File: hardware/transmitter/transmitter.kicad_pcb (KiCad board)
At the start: 2 copper layers, 85.1 x 53.3 mm, 23 parts, among them J1 Screw_Terminal_01x05, P5 Digital, P6 Analog, U1 uA7805, U2 TMP36, U3 JSN-SR04T-2.0, U4 MAX3232

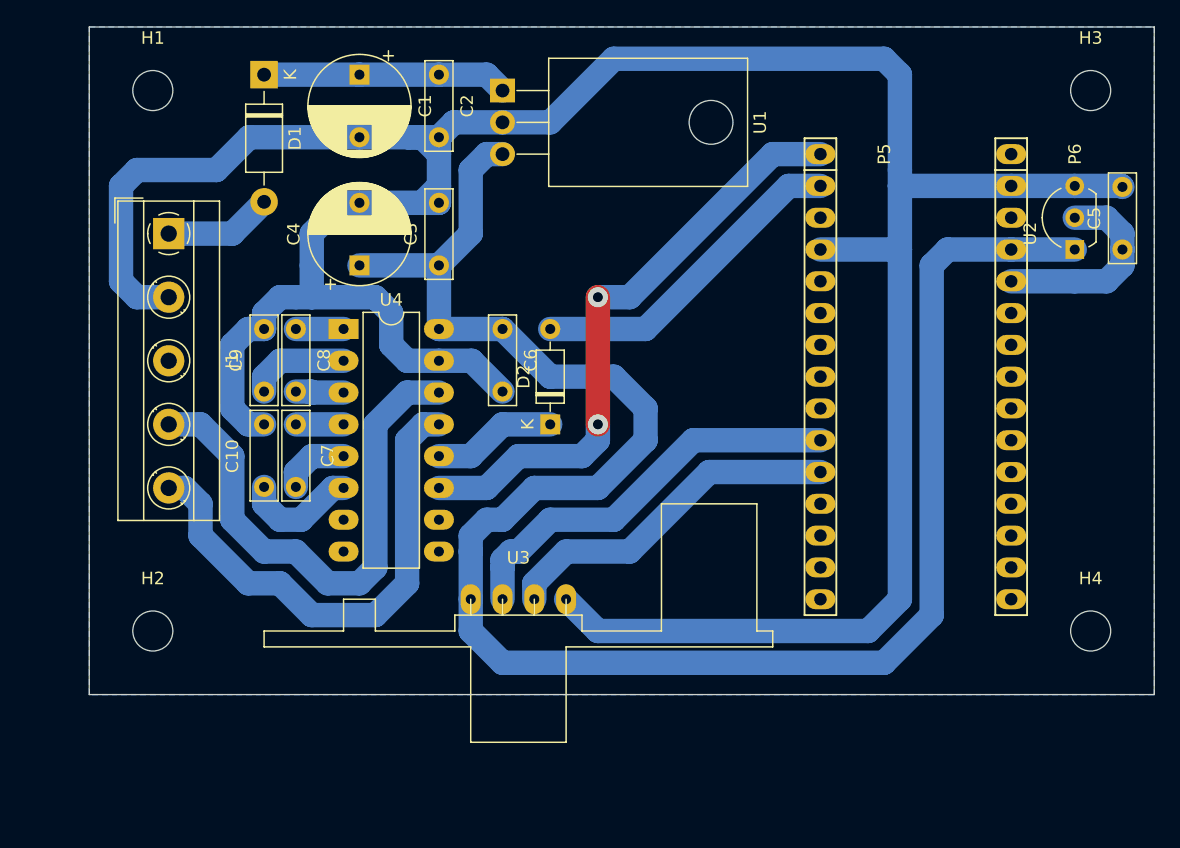
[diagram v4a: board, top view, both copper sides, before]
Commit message: improved silk + additional .pdfs
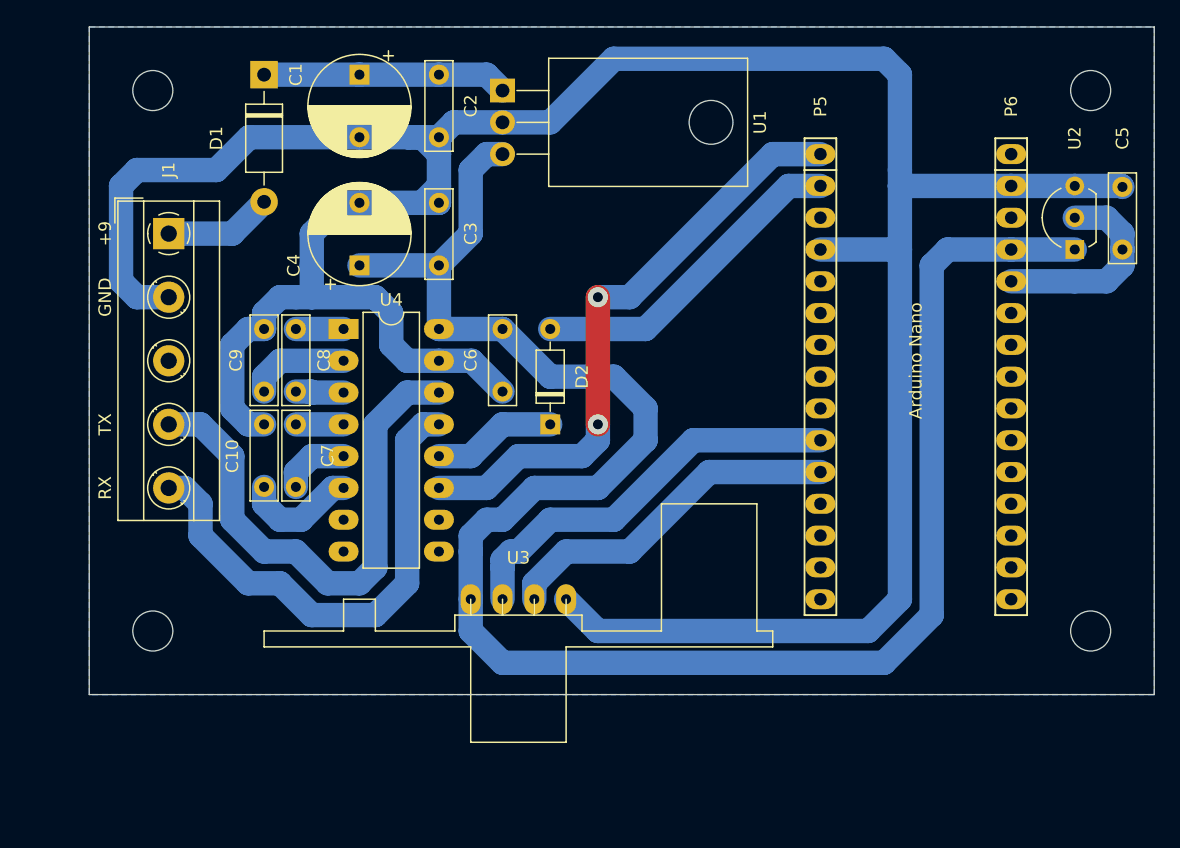
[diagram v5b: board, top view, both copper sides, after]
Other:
- board text added: "+9"
- board text added: "Arduino Nano"
- board text added: "GND"
- board text added: "RX"
- board text added: "TX"
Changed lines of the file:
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@@
   (general
     (thickness 1.6)
-    (drawings 6)
+    (drawings 13)
     (tracks 162)
     (zones 0)
@@
     (44 Edge.Cuts user)
     (45 Margin user)
-    (46 B.CrtYd user)
+    (46 B.CrtYd user hide)
     (47 F.CrtYd user)
-    (48 B.Fab user)
-    (49 F.Fab user)
+    (48 B.Fab user hide)
+    (49 F.Fab user hide)
   )
   (setup
@@
     (descr "TO-92L leads in-line (large body variant of TO-92), also known as TO-226, wide, drill 0.75mm (see https://www.diodes.com/assets/Package-Files/TO92L.pdf and http://www.ti.com/lit/an/snoa059/snoa059.pdf)")
     (tags "TO-92L Inline Wide transistor")
-    (fp_text reference U2 (at 1.27 -3.56 90) (layer F.SilkS)
+    (fp_text reference U2 (at 8.89 0 90) (layer F.SilkS)
       (effects (font (size 1 1) (thickness 0.15)))
     )
@@
     (descr "Through hole socket strip")
     (tags "socket strip")
-    (fp_text reference P6 (at 0 -5.1 90) (layer F.SilkS)
+    (fp_text reference P6 (at -3.81 0 90) (layer F.SilkS)
       (effects (font (size 1 1) (thickness 0.15)))
     )
@@
     (descr "Through hole socket strip")
     (tags "socket strip")
-    (fp_text reference P5 (at 0 -5.1 90) (layer F.SilkS)
+    (fp_text reference P5 (at -3.81 0 90) (layer F.SilkS)
       (effects (font (size 1 1) (thickness 0.15)))
     )
@@
     (descr "terminal block Metz Connect Type101_RT01605HBWC, 5 pins, pitch 5.08mm, size 25.4x8mm^2, drill diamater 1.3mm, pad diameter 2.5mm, see http://www.metz-connect.com/de/system/files/productfiles/Datenblatt_311011_RT016xxHBWC_OFF-022771S.pdf, script-generated using https://github.com/pointhi/kicad-footprint-generator/scripts/TerminalBlock_MetzConnect")
     (tags "THT terminal block Metz Connect Type101_RT01605HBWC pitch 5.08mm size 25.4x8mm^2 drill 1.3mm pad 2.5mm")
-    (fp_text reference J1 (at 10.16 -5.06 90) (layer F.SilkS)
+    (fp_text reference J1 (at -5.08 0 90) (layer F.SilkS)
       (effects (font (size 1 1) (thickness 0.15)))
     )
@@
     (tags "mounting hole 3.2mm no annular m3")
     (attr virtual)
-    (fp_text reference H4 (at 0 -4.2) (layer F.SilkS)
+    (fp_text reference H4 (at 0 -4.2) (layer F.SilkS) hide
       (effects (font (size 1 1) (thickness 0.15)))
     )
@@
     (fp_circle (center 0 0) (end 3.45 0) (layer F.CrtYd) (width 0.05))
     (fp_circle (center 0 0) (end 3.2 0) (layer Cmts.User) (width 0.15))
-    (fp_text user %R (at 0.3 0) (layer F.Fab)
+    (fp_text user %R (at 0.3 0) (layer F.SilkS) hide
       (effects (font (size 1 1) (thickness 0.15)))
     )
@@
     (tags "mounting hole 3.2mm no annular m3")
     (attr virtual)
-    (fp_text reference H3 (at 0 -4.2) (layer F.SilkS)
+    (fp_text reference H3 (at 0 -4.2) (layer F.SilkS) hide
       (effects (font (size 1 1) (thickness 0.15)))
     )
@@
     (tags "mounting hole 3.2mm no annular m3")
     (attr virtual)
-    (fp_text reference H2 (at 0 -4.2) (layer F.SilkS)
+    (fp_text reference H2 (at 0 -4.2) (layer F.SilkS) hide
       (effects (font (size 1 1) (thickness 0.15)))
     )
@@
     (tags "mounting hole 3.2mm no annular m3")
     (attr virtual)
-    (fp_text reference H1 (at 0 -4.2) (layer F.SilkS)
+    (fp_text reference H1 (at 0 -4.2) (layer F.SilkS) hide
       (effects (font (size 1 1) (thickness 0.15)))
     )
@@
     (descr "Diode, DO-35_SOD27 series, Axial, Horizontal, pin pitch=7.62mm, , length*diameter=4*2mm^2, , http://www.diodes.com/_files/packages/DO-35.pdf")
     (tags "Diode DO-35_SOD27 series Axial Horizontal pin pitch 7.62mm  length 4mm diameter 2mm")
-    (fp_text reference D2 (at 3.81 -2.12 90) (layer F.SilkS)
+    (fp_text reference D2 (at 3.81 2.54 90) (layer F.SilkS)
       (effects (font (size 1 1) (thickness 0.15)))
     )
@@
       (effects (font (size 1 1) (thickness 0.15)))
     )
-    (fp_text user K (at 0 -1.8 90) (layer F.SilkS)
+    (fp_text user K (at 0 -1.8 90) (layer F.SilkS) hide
       (effects (font (size 1 1) (thickness 0.15)))
     )
@@
     (descr "Diode, DO-41_SOD81 series, Axial, Horizontal, pin pitch=10.16mm, , length*diameter=5.2*2.7mm^2, , http://www.diodes.com/_files/packages/DO-41%20(Plastic).pdf")
     (tags "Diode DO-41_SOD81 series Axial Horizontal pin pitch 10.16mm  length 5.2mm diameter 2.7mm")
-    (fp_text reference D1 (at 5.08 -2.47 90) (layer F.SilkS)
+    (fp_text reference D1 (at 5.08 3.81 90) (layer F.SilkS)
       (effects (font (size 1 1) (thickness 0.15)))
     )
@@
       (effects (font (size 1 1) (thickness 0.15)))
     )
-    (fp_text user K (at 0 -2.1 90) (layer F.SilkS)
+    (fp_text user K (at 0 -2.1 90) (layer F.SilkS) hide
       (effects (font (size 1 1) (thickness 0.15)))
     )
@@
     (descr "C, Rect series, Radial, pin pitch=5.00mm, , length*width=7*2mm^2, Capacitor")
     (tags "C Rect series Radial pin pitch 5.00mm  length 7mm width 2mm Capacitor")
-    (fp_text reference C6 (at 2.5 -2.25 90) (layer F.SilkS)
+    (fp_text reference C6 (at 2.5 2.54 90) (layer F.SilkS)
       (effects (font (size 1 1) (thickness 0.15)))
     )
@@
     (descr "C, Rect series, Radial, pin pitch=5.00mm, , length*width=7*2mm^2, Capacitor")
     (tags "C Rect series Radial pin pitch 5.00mm  length 7mm width 2mm Capacitor")
-    (fp_text reference C5 (at 2.5 -2.25 90) (layer F.SilkS)
+    (fp_text reference C5 (at 8.89 0 90) (layer F.SilkS)
       (effects (font (size 1 1) (thickness 0.15)))
     )
@@
     (descr "CP, Radial series, Radial, pin pitch=5.00mm, , diameter=8mm, Electrolytic Capacitor")
     (tags "CP Radial series Radial pin pitch 5.00mm  diameter 8mm Electrolytic Capacitor")
-    (fp_text reference C4 (at 2.5 -5.25 90) (layer F.SilkS)
+    (fp_text reference C4 (at 0 -5.25 90) (layer F.SilkS)
       (effects (font (size 1 1) (thickness 0.15)))
     )
@@
     (descr "C, Rect series, Radial, pin pitch=5.00mm, , length*width=7*2mm^2, Capacitor")
     (tags "C Rect series Radial pin pitch 5.00mm  length 7mm width 2mm Capacitor")
-    (fp_text reference C3 (at 2.5 -2.25 90) (layer F.SilkS)
+    (fp_text reference C3 (at 2.54 2.54 90) (layer F.SilkS)
       (effects (font (size 1 1) (thickness 0.15)))
     )
@@
     (descr "C, Rect series, Radial, pin pitch=5.00mm, , length*width=7*2mm^2, Capacitor")
     (tags "C Rect series Radial pin pitch 5.00mm  length 7mm width 2mm Capacitor")
-    (fp_text reference C2 (at 2.5 -2.25 90) (layer F.SilkS)
+    (fp_text reference C2 (at 2.5 -2.54 90) (layer F.SilkS)
       (effects (font (size 1 1) (thickness 0.15)))
     )
@@
     (descr "CP, Radial series, Radial, pin pitch=5.00mm, , diameter=8mm, Electrolytic Capacitor")
     (tags "CP Radial series Radial pin pitch 5.00mm  diameter 8mm Electrolytic Capacitor")
-    (fp_text reference C1 (at 2.5 -5.25 90) (layer F.SilkS)
+    (fp_text reference C1 (at 0 5.08 90) (layer F.SilkS)
       (effects (font (size 1 1) (thickness 0.15)))
     )
@@
     )
   )
+  (gr_text "Arduino Nano" (at 134.62 77.47 90) (layer F.SilkS)
+    (effects (font (size 1 1) (thickness 0.15)))
+  )
+  (gr_text RX (at 69.85 87.63 90) (layer F.SilkS)
+    (effects (font (size 1 1) (thickness 0.15)))
+  )
+  (gr_text TX (at 69.85 82.55 90) (layer F.SilkS)
+    (effects (font (size 1 1) (thickness 0.15)))
+  )
+  (gr_text GND (at 69.85 72.39 90) (layer F.SilkS)
+    (effects (font (size 1 1) (thickness 0.15)))
+  )
+  (gr_text +9 (at 69.85 67.31 90) (layer F.SilkS)
+    (effects (font (size 1 1) (thickness 0.15)))
+  )
+  (dimension 74.93 (width 0.15) (layer Dwgs.User)
+    (gr_text "74,930 mm" (at 111.125 114.33) (layer Dwgs.User)
+      (effects (font (size 1 1) (thickness 0.15)))
+    )
+    (feature1 (pts (xy 148.59 99.06) (xy 148.59 113.616421)))
+    (feature2 (pts (xy 73.66 99.06) (xy 73.66 113.616421)))
+    (crossbar (pts (xy 73.66 113.03) (xy 148.59 113.03)))
+    (arrow1a (pts (xy 148.59 113.03) (xy 147.463496 113.616421)))
+    (arrow1b (pts (xy 148.59 113.03) (xy 147.463496 112.443579)))
+    (arrow2a (pts (xy 73.66 113.03) (xy 74.786504 113.616421)))
+    (arrow2b (pts (xy 73.66 113.03) (xy 74.786504 112.443579)))
+  )
+  (dimension 43.18 (width 0.15) (layer Dwgs.User)
+    (gr_text "43,180 mm" (at 62.2 77.47 90) (layer Dwgs.User)
+      (effects (font (size 1 1) (thickness 0.15)))
+    )
+    (feature1 (pts (xy 73.66 55.88) (xy 62.913579 55.88)))
+    (feature2 (pts (xy 73.66 99.06) (xy 62.913579 99.06)))
+    (crossbar (pts (xy 63.5 99.06) (xy 63.5 55.88)))
+    (arrow1a (pts (xy 63.5 55.88) (xy 64.086421 57.006504)))
+    (arrow1b (pts (xy 63.5 55.88) (xy 62.913579 57.006504)))
+    (arrow2a (pts (xy 63.5 99.06) (xy 64.086421 97.933496)))
+    (arrow2b (pts (xy 63.5 99.06) (xy 62.913579 97.933496)))
+  )
   (gr_line (start 68.58 104.14) (end 68.58 50.8) (layer Edge.Cuts) (width 0.1))
